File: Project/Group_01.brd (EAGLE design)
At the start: 71.1 x 54.3 mm, 29 parts, among them J1 POWER_JACKPTH_LOCK, U1 +12v, U4 TMUX1208

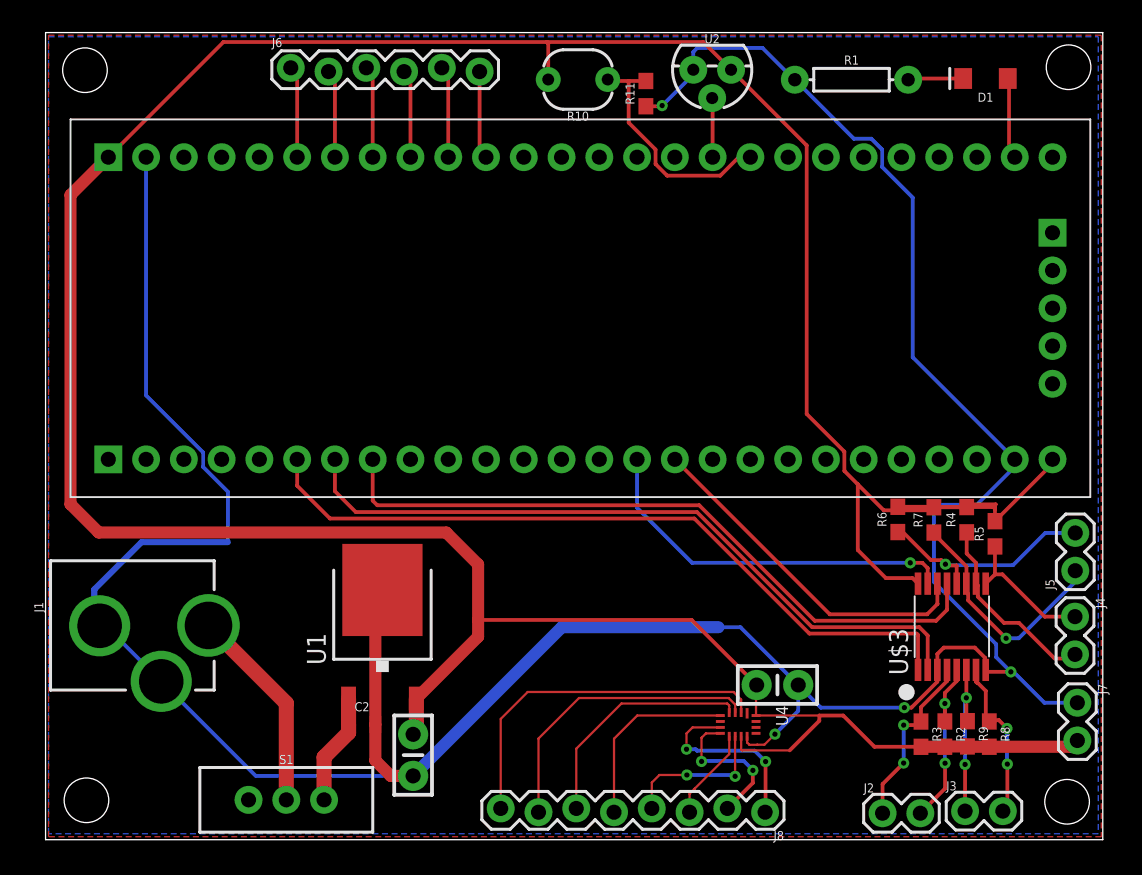
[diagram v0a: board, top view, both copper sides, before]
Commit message: changed position of jumpers
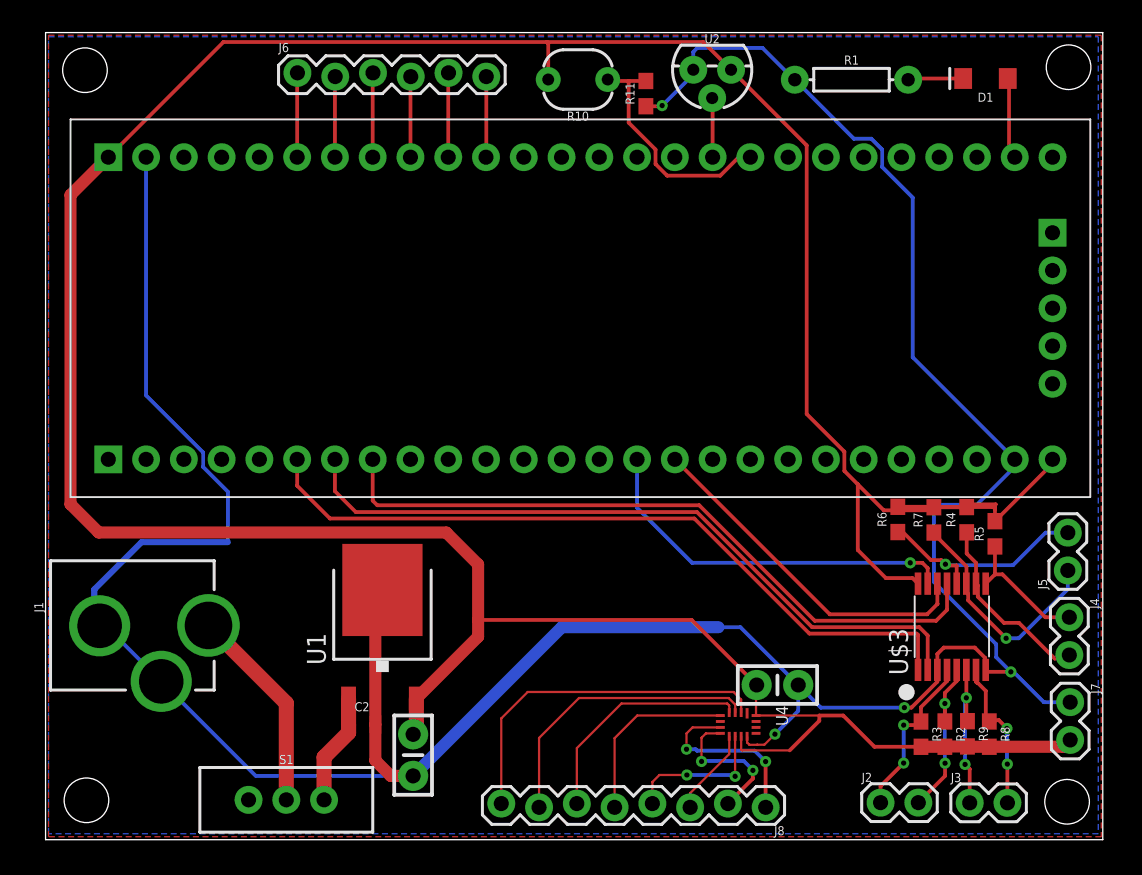
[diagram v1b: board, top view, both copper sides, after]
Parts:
- moved J2 0.72 mm to (56.2, 2.49)
- moved J3 0.64 mm to (62.1, 2.48)
- moved J6 0.56 mm to (16.9, 51.6)
- moved J5 0.50 mm to (68.7, 18.1)
- moved J7 0.48 mm to (68.9, 9.25)
- moved J4 0.39 mm to (68.9, 15.0)
- moved J8 0.33 mm to (48.4, 2.30)
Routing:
- net I2C_SCL_1: track 11.1 -> 10.5 mm
- net I2C_SDA_0: track 12.0 -> 11.3 mm
- net I2C_SCL_0: track 11.9 -> 11.2 mm
- net N$2: track 6.19 -> 5.68 mm
- net N$7: track 5.93 -> 5.43 mm
- net N$4: track 6.19 -> 5.68 mm
- net N$3: track 5.93 -> 5.43 mm
- net N$6: track 6.19 -> 5.68 mm
- net N$5: track 5.93 -> 5.43 mm

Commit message: Silkscreen improved
It's the tname layer
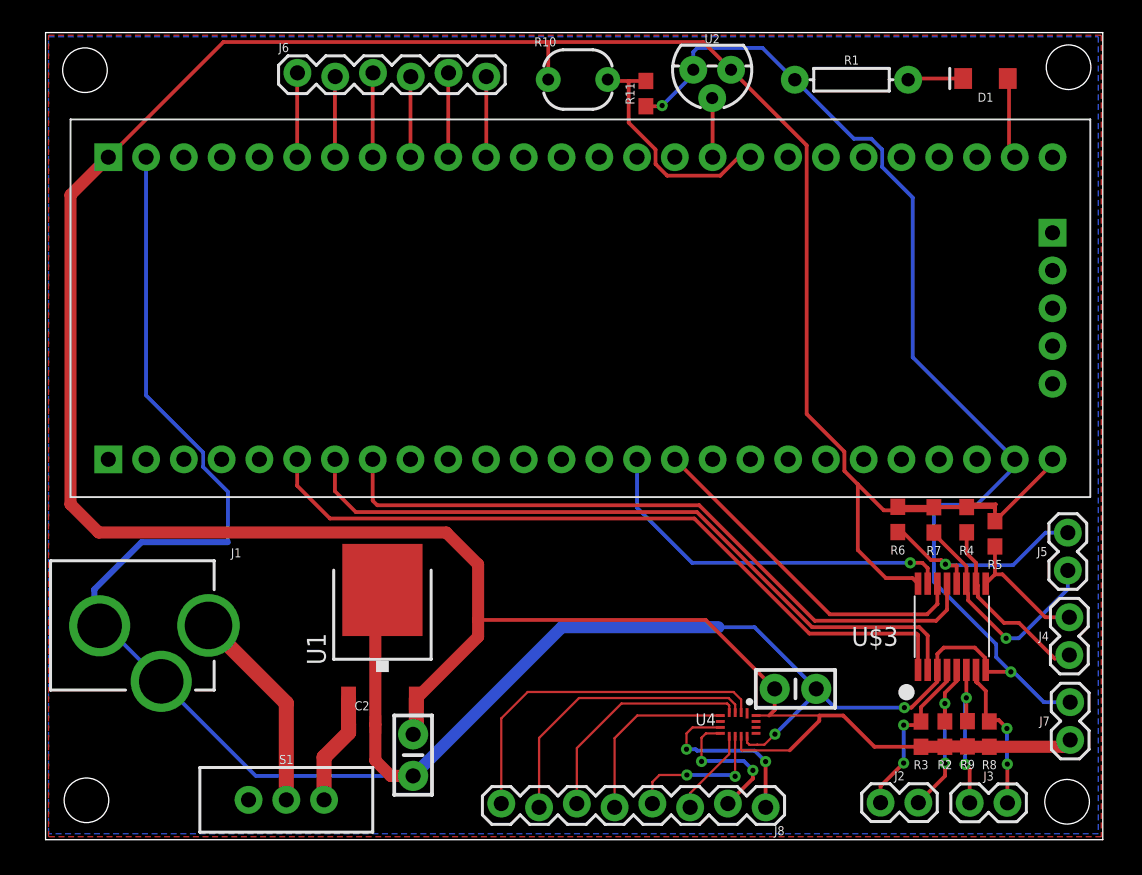
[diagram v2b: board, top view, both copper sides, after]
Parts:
- moved C3 1.24 mm to (50.4, 10.1)
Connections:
- net 5V: now also U4.11, U4.16; no longer U4.EN, U4.VDD
- net GND: now also U4.12; no longer U4.GND
- net MUX_A0/1.3C: now also U4.15; no longer U4.A0
- net MUX_A1/1.4C: now also U4.14; no longer U4.A1
- net MUX_A2/1.4C: now also U4.13; no longer U4.A2
- net MUX_OUT/1.4C: now also U4.6; no longer U4.D
- net N$10: now also U4.2; no longer U4.S1
- net N$11: now also U4.3; no longer U4.S2
- net N$12: now also U4.4; no longer U4.S3
- net N$13: now also U4.5; no longer U4.S4
- net N$14: now also U4.10; no longer U4.S5
- net N$15: now also U4.9; no longer U4.S6
- net N$16: now also U4.8; no longer U4.S7
- net N$17: now also U4.7; no longer U4.S8
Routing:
- net 5V: track 234.1 -> 235.3 mm

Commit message: Changed name
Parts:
- renumbered U$3 to U3
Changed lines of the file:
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@@
 <attribute name="VALUE" x="41.13478125" y="50.174271875" size="0.6096" layer="27" font="vector" ratio="20" rot="R90" align="top-center"/>
 </element>
-<element name="U$3" library="Group_01_Library" package="TSSOP16" value="TCA9546A" x="60.95" y="14.32" smashed="yes" rot="R90">
+<element name="U3" library="Group_01_Library" package="TSSOP16" value="TCA9546A" x="60.95" y="14.32" smashed="yes" rot="R90">
 <attribute name="NAME" x="57.347734375" y="13.668865625" size="1.27" layer="25" align="center-right"/>
 </element>
@@
 <contactref element="C1" pad="2"/>
 <contactref element="U1" pad="3"/>
-<contactref element="U$3" pad="8"/>
-<contactref element="U$3" pad="3"/>
+<contactref element="U3" pad="8"/>
+<contactref element="U3" pad="3"/>
 <contactref element="U$2" pad="28"/>
 <contactref element="R1" pad="P$1"/>
@@
 <contactref element="U1" pad="2"/>
 <contactref element="C1" pad="1"/>
-<contactref element="U$3" pad="16"/>
+<contactref element="U3" pad="16"/>
 <contactref element="R2" pad="2"/>
 <contactref element="R3" pad="2"/>
@@
 </signal>
 <signal name="I2C_SCL_0">
-<contactref element="U$3" pad="5"/>
+<contactref element="U3" pad="5"/>
 <contactref element="R2" pad="1"/>
 <contactref element="J2" pad="2"/>
@@
 <signal name="I2C_SDA_0">
 <contactref element="R3" pad="1"/>
-<contactref element="U$3" pad="4"/>
+<contactref element="U3" pad="4"/>
 <contactref element="J2" pad="1"/>
 <wire x1="60.625" y1="11.42" x2="60.625" y2="10.66395" width="0.254" layer="1"/>
@@
 </signal>
 <signal name="I2C_SDA_1">
-<contactref element="U$3" pad="6"/>
+<contactref element="U3" pad="6"/>
 <contactref element="R9" pad="1"/>
 <contactref element="J3" pad="1"/>
@@
 <signal name="I2C_SCL_1">
 <contactref element="R8" pad="1"/>
-<contactref element="U$3" pad="7"/>
+<contactref element="U3" pad="7"/>
 <contactref element="J3" pad="2"/>
 <wire x1="63.47" y1="7.95" x2="63.2333" y2="8.1867" width="0.254" layer="1"/>
@@
 </signal>
 <signal name="I2C_SDA_2">
-<contactref element="U$3" pad="9"/>
+<contactref element="U3" pad="9"/>
 <contactref element="R5" pad="1"/>
 <contactref element="J4" pad="1"/>
@@
 <signal name="I2C_SCL_2">
 <contactref element="R4" pad="1"/>
-<contactref element="U$3" pad="10"/>
+<contactref element="U3" pad="10"/>
 <contactref element="J4" pad="2"/>
 <wire x1="61.946959375" y1="20.669490625" x2="61.946959375" y2="19.24795" width="0.254" layer="1"/>
@@
 </signal>
 <signal name="I2C_SCL_3">
-<contactref element="U$3" pad="12"/>
+<contactref element="U3" pad="12"/>
 <contactref element="R6" pad="1"/>
 <contactref element="J5" pad="2"/>
@@
 </signal>
 <signal name="I2C_SDA_3">
-<contactref element="U$3" pad="11"/>
+<contactref element="U3" pad="11"/>
 <contactref element="R7" pad="1"/>
 <contactref element="J5" pad="1"/>
@@
 </signal>
 <signal name="I2C_SDA">
-<contactref element="U$3" pad="15"/>
+<contactref element="U3" pad="15"/>
 <contactref element="U$2" pad="15"/>
 <wire x1="59.325" y1="17.22" x2="59.324240625" y2="17.220759375" width="0.254" layer="1"/>
@@
 </signal>
 <signal name="I2C_SCL">
-<contactref element="U$3" pad="14"/>
+<contactref element="U3" pad="14"/>
 <contactref element="U$2" pad="16"/>
 <wire x1="59.975" y1="17.22" x2="59.975" y2="15.866859375" width="0.254" layer="1"/>
@@
 </signal>
 <signal name="I2C_A2">
-<contactref element="U$3" pad="13"/>
+<contactref element="U3" pad="13"/>
 <contactref element="U$2" pad="8"/>
 <wire x1="60.625" y1="17.22" x2="60.625" y2="15.45490625" width="0.254" layer="1"/>
@@
 </signal>
 <signal name="I2C_A1">
-<contactref element="U$3" pad="2"/>
+<contactref element="U3" pad="2"/>
 <contactref element="U$2" pad="7"/>
 <wire x1="59.325" y1="11.42" x2="59.325" y2="13.730478125" width="0.254" layer="1"/>
@@
 </signal>
 <signal name="I2C_A0">
-<contactref element="U$3" pad="1"/>
+<contactref element="U3" pad="1"/>
 <contactref element="U$2" pad="6"/>
 <wire x1="58.675" y1="11.42" x2="58.675" y2="13.76981875" width="0.254" layer="1"/>

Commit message: Revert "Changed name"
This reverts commit 609342ddda2755176251b6021189b0587eea2b8d.
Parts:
- renumbered U3 to U$3
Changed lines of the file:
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@@
 <attribute name="VALUE" x="41.13478125" y="50.174271875" size="0.6096" layer="27" font="vector" ratio="20" rot="R90" align="top-center"/>
 </element>
-<element name="U3" library="Group_01_Library" package="TSSOP16" value="TCA9546A" x="60.95" y="14.32" smashed="yes" rot="R90">
+<element name="U$3" library="Group_01_Library" package="TSSOP16" value="TCA9546A" x="60.95" y="14.32" smashed="yes" rot="R90">
 <attribute name="NAME" x="57.347734375" y="13.668865625" size="1.27" layer="25" align="center-right"/>
 </element>
@@
 <contactref element="C1" pad="2"/>
 <contactref element="U1" pad="3"/>
-<contactref element="U3" pad="8"/>
-<contactref element="U3" pad="3"/>
+<contactref element="U$3" pad="8"/>
+<contactref element="U$3" pad="3"/>
 <contactref element="U$2" pad="28"/>
 <contactref element="R1" pad="P$1"/>
@@
 <contactref element="U1" pad="2"/>
 <contactref element="C1" pad="1"/>
-<contactref element="U3" pad="16"/>
+<contactref element="U$3" pad="16"/>
 <contactref element="R2" pad="2"/>
 <contactref element="R3" pad="2"/>
@@
 </signal>
 <signal name="I2C_SCL_0">
-<contactref element="U3" pad="5"/>
+<contactref element="U$3" pad="5"/>
 <contactref element="R2" pad="1"/>
 <contactref element="J2" pad="2"/>
@@
 <signal name="I2C_SDA_0">
 <contactref element="R3" pad="1"/>
-<contactref element="U3" pad="4"/>
+<contactref element="U$3" pad="4"/>
 <contactref element="J2" pad="1"/>
 <wire x1="60.625" y1="11.42" x2="60.625" y2="10.66395" width="0.254" layer="1"/>
@@
 </signal>
 <signal name="I2C_SDA_1">
-<contactref element="U3" pad="6"/>
+<contactref element="U$3" pad="6"/>
 <contactref element="R9" pad="1"/>
 <contactref element="J3" pad="1"/>
@@
 <signal name="I2C_SCL_1">
 <contactref element="R8" pad="1"/>
-<contactref element="U3" pad="7"/>
+<contactref element="U$3" pad="7"/>
 <contactref element="J3" pad="2"/>
 <wire x1="63.47" y1="7.95" x2="63.2333" y2="8.1867" width="0.254" layer="1"/>
@@
 </signal>
 <signal name="I2C_SDA_2">
-<contactref element="U3" pad="9"/>
+<contactref element="U$3" pad="9"/>
 <contactref element="R5" pad="1"/>
 <contactref element="J4" pad="1"/>
@@
 <signal name="I2C_SCL_2">
 <contactref element="R4" pad="1"/>
-<contactref element="U3" pad="10"/>
+<contactref element="U$3" pad="10"/>
 <contactref element="J4" pad="2"/>
 <wire x1="61.946959375" y1="20.669490625" x2="61.946959375" y2="19.24795" width="0.254" layer="1"/>
@@
 </signal>
 <signal name="I2C_SCL_3">
-<contactref element="U3" pad="12"/>
+<contactref element="U$3" pad="12"/>
 <contactref element="R6" pad="1"/>
 <contactref element="J5" pad="2"/>
@@
 </signal>
 <signal name="I2C_SDA_3">
-<contactref element="U3" pad="11"/>
+<contactref element="U$3" pad="11"/>
 <contactref element="R7" pad="1"/>
 <contactref element="J5" pad="1"/>
@@
 </signal>
 <signal name="I2C_SDA">
-<contactref element="U3" pad="15"/>
+<contactref element="U$3" pad="15"/>
 <contactref element="U$2" pad="15"/>
 <wire x1="59.325" y1="17.22" x2="59.324240625" y2="17.220759375" width="0.254" layer="1"/>
@@
 </signal>
 <signal name="I2C_SCL">
-<contactref element="U3" pad="14"/>
+<contactref element="U$3" pad="14"/>
 <contactref element="U$2" pad="16"/>
 <wire x1="59.975" y1="17.22" x2="59.975" y2="15.866859375" width="0.254" layer="1"/>
@@
 </signal>
 <signal name="I2C_A2">
-<contactref element="U3" pad="13"/>
+<contactref element="U$3" pad="13"/>
 <contactref element="U$2" pad="8"/>
 <wire x1="60.625" y1="17.22" x2="60.625" y2="15.45490625" width="0.254" layer="1"/>
@@
 </signal>
 <signal name="I2C_A1">
-<contactref element="U3" pad="2"/>
+<contactref element="U$3" pad="2"/>
 <contactref element="U$2" pad="7"/>
 <wire x1="59.325" y1="11.42" x2="59.325" y2="13.730478125" width="0.254" layer="1"/>
@@
 </signal>
 <signal name="I2C_A0">
-<contactref element="U3" pad="1"/>
+<contactref element="U$3" pad="1"/>
 <contactref element="U$2" pad="6"/>
 <wire x1="58.675" y1="11.42" x2="58.675" y2="13.76981875" width="0.254" layer="1"/>

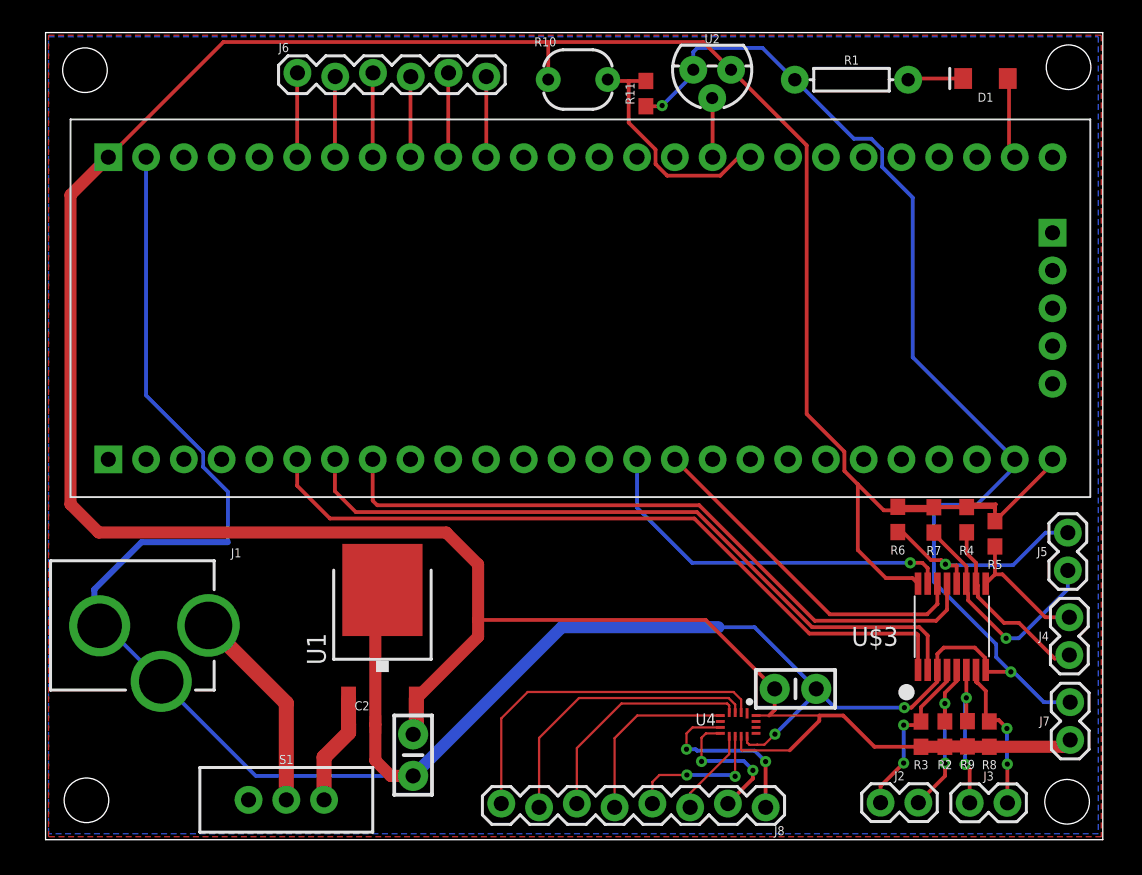
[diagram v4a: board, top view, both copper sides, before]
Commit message: 5V on bottom and GND on top
Corrected, it was the opposite before!!
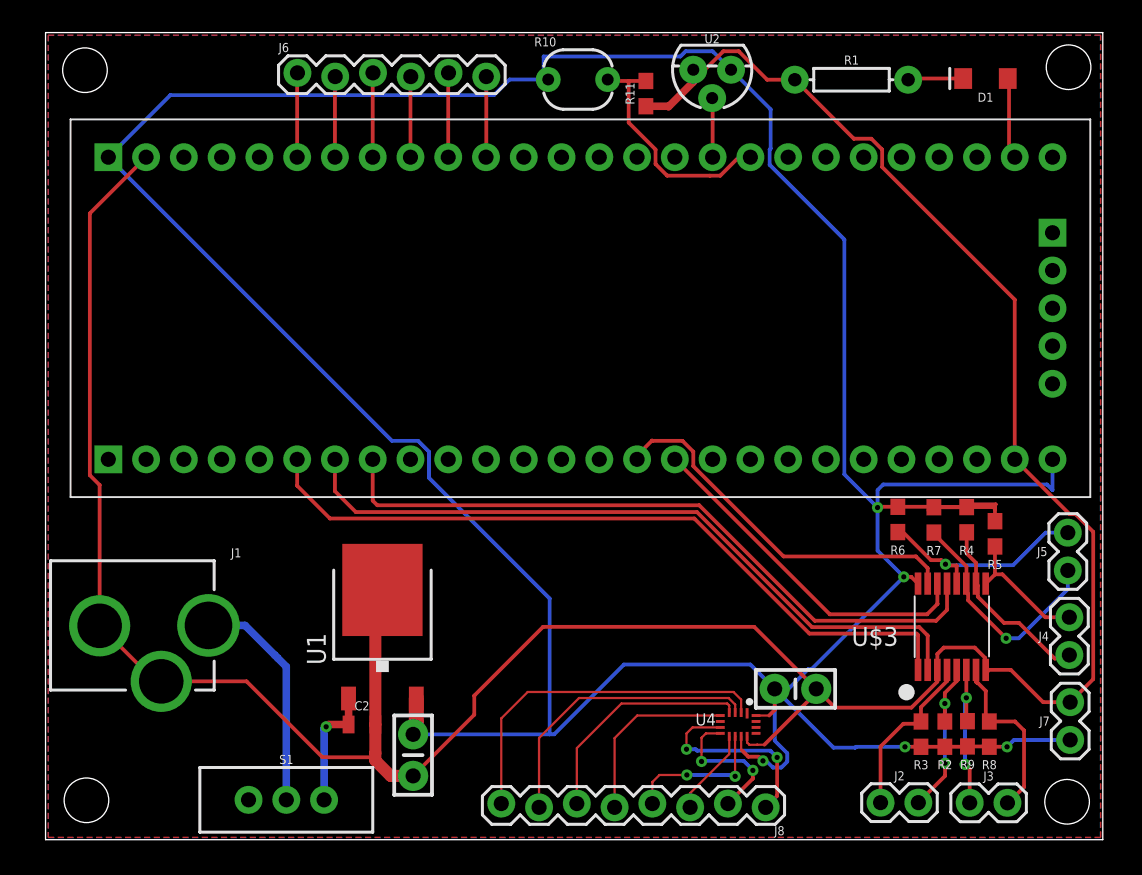
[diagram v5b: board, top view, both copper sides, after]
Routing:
- net GND: track 209.4 -> 198.5 mm, vias 4 -> 0
- net 5V: track 235.3 -> 244.6 mm, vias 0 -> 5
- net N$1: track 13.9 -> 15.3 mm
- net I2C_SCL_1: track 10.5 -> 11.8 mm, vias 2 -> 0
- net N$17: track 12.3 -> 13.5 mm
- net 12V: track 7.50 -> 8.29 mm, vias 0 -> 1
- net I2C_SDA: track 25.5 -> 25.4 mm, vias 1 -> 0
- net I2C_SDA_0: track 11.3 -> 11.4 mm, vias 2 -> 0
- added copper zone on layer 16, net 5V
- added copper zone on layer 1, net GND
- removed copper zone on layer 1, net 5V
- removed copper zone on layer 16, net GND

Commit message: Schematic on 2 sheets
And other minor improvements on the board, added readme file
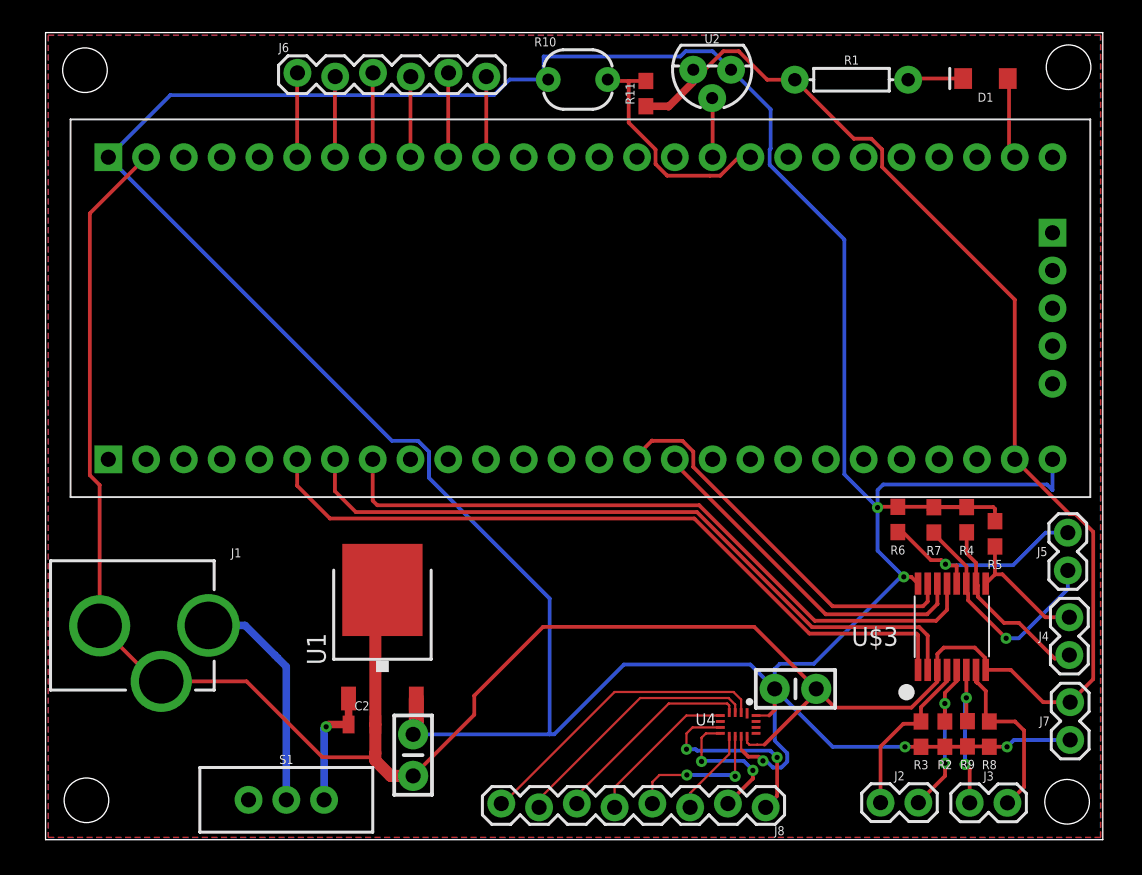
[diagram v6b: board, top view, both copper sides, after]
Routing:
- net N$10: track 23.7 -> 20.3 mm
- net N$11: track 19.7 -> 17.3 mm
- net N$13: track 12.4 -> 10.5 mm
- net N$12: track 15.7 -> 13.9 mm
- net 5V: track 244.6 -> 242.8 mm
- net I2C_SDA: track 25.4 -> 26.8 mm
- net GND: track 198.5 -> 198.0 mm
